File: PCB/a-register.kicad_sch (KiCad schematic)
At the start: 23 parts, among them U48 74LS245, U49 74LS173, U50 74LS173

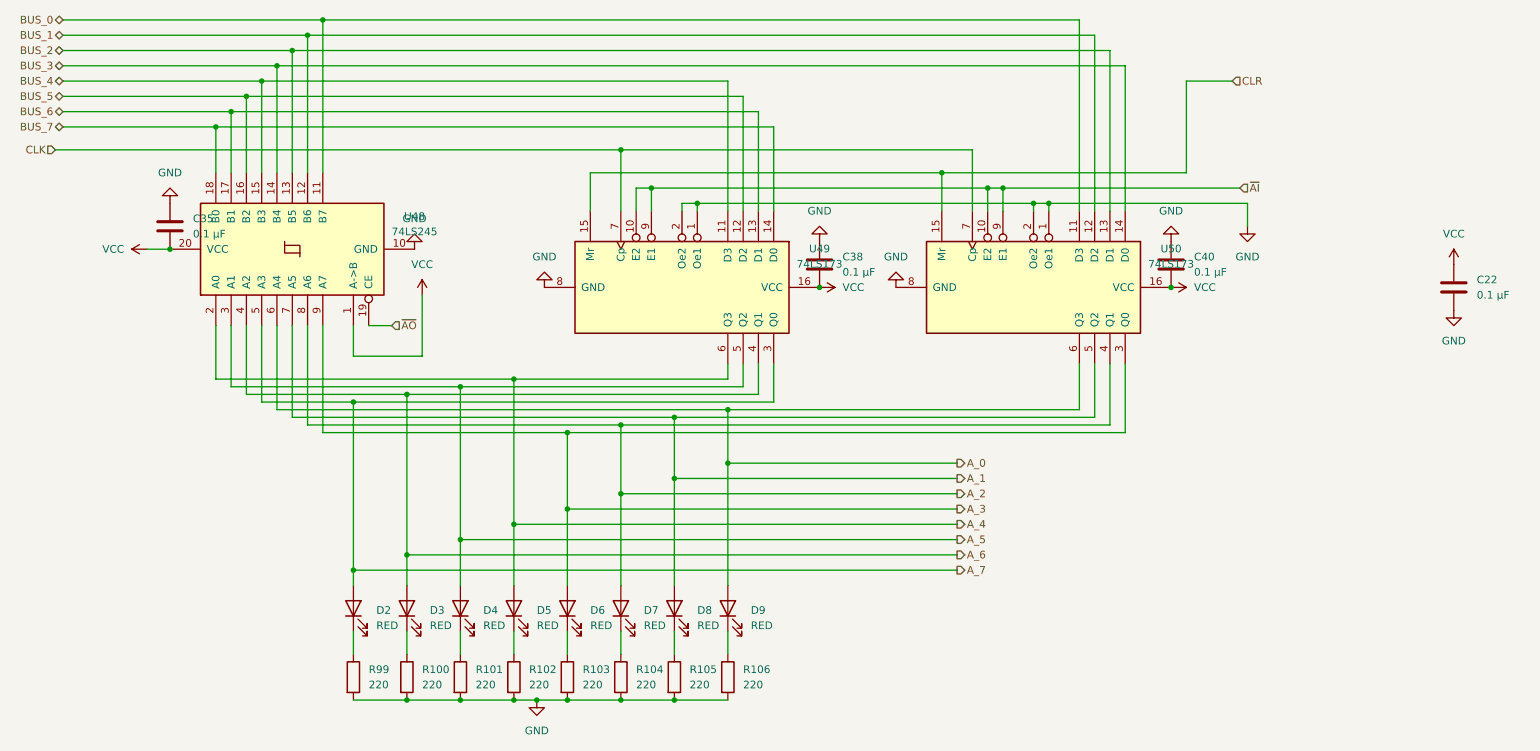
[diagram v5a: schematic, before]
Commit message: Redoing PCB layout and fixed some signal flow convention errors
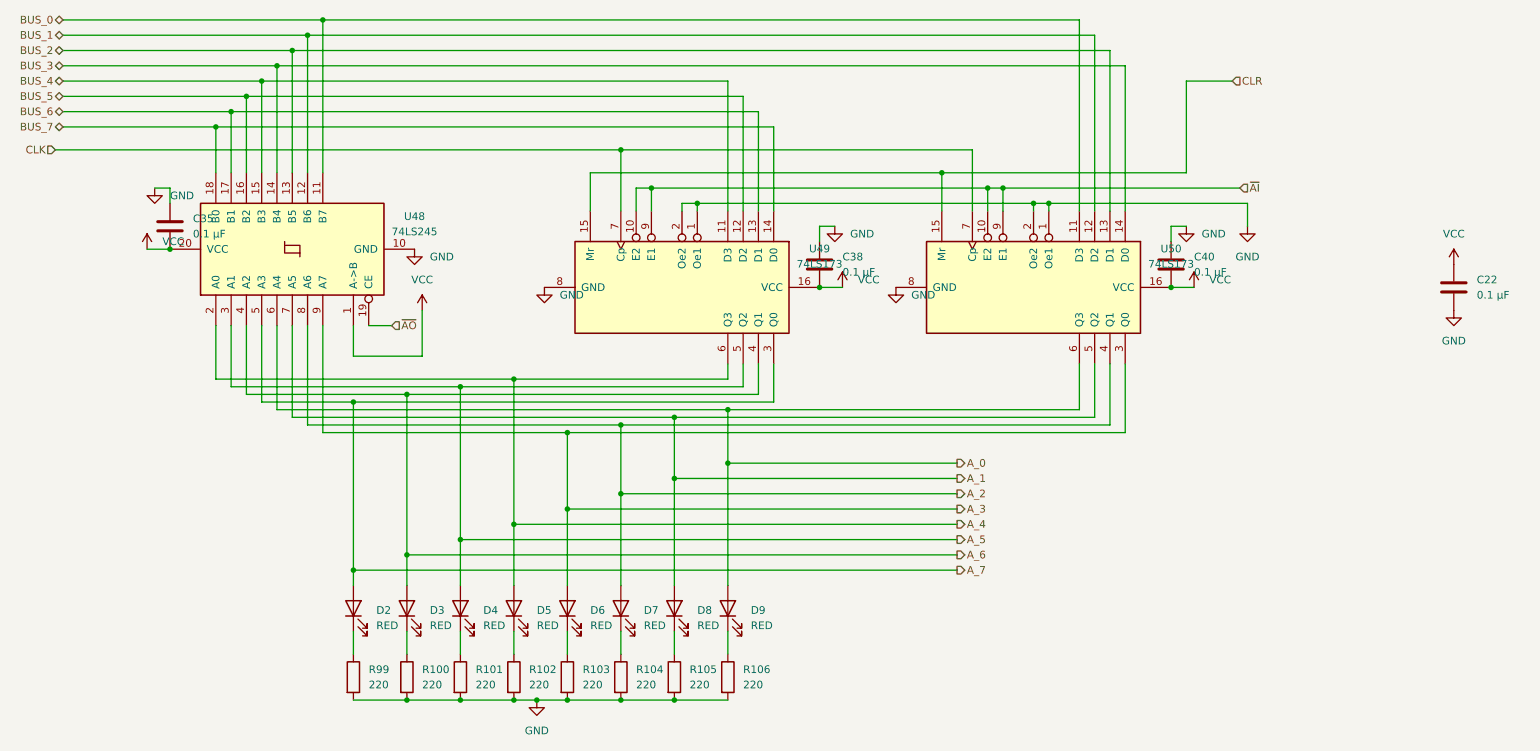
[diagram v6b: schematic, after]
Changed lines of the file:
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@@
 	(wire
 		(pts
+			(xy 217.17 64.77) (xy 213.36 64.77)
+		)
+		(stroke
+			(width 0)
+			(type default)
+		)
+	)
+	(wire
+		(pts
 			(xy 121.92 121.92) (xy 121.92 125.73)
 		)
@@
 	(wire
 		(pts
+			(xy 157.48 54.61) (xy 154.94 54.61)
+		)
+		(stroke
+			(width 0)
+			(type default)
+		)
+	)
+	(wire
+		(pts
 			(xy 104.14 121.92) (xy 104.14 125.73)
 		)
@@
 	(wire
 		(pts
+			(xy 154.94 54.61) (xy 154.94 57.15)
+		)
+		(stroke
+			(width 0)
+			(type default)
+		)
+	)
+	(wire
+		(pts
+			(xy 46.99 48.26) (xy 46.99 50.8)
+		)
+		(stroke
+			(width 0)
+			(type default)
+		)
+	)
+	(wire
+		(pts
 			(xy 203.2 25.4) (xy 203.2 52.07)
 		)
@@
 	(wire
 		(pts
+			(xy 158.75 64.77) (xy 154.94 64.77)
+		)
+		(stroke
+			(width 0)
+			(type default)
+		)
+	)
+	(wire
+		(pts
 			(xy 59.69 33.02) (xy 59.69 45.72)
 		)
@@
 	(wire
 		(pts
+			(xy 44.45 48.26) (xy 46.99 48.26)
+		)
+		(stroke
+			(width 0)
+			(type default)
+		)
+	)
+	(wire
+		(pts
 			(xy 67.31 25.4) (xy 203.2 25.4)
 		)
@@
 	(wire
 		(pts
+			(xy 213.36 54.61) (xy 213.36 57.15)
+		)
+		(stroke
+			(width 0)
+			(type default)
+		)
+	)
+	(wire
+		(pts
 			(xy 69.85 22.86) (xy 69.85 45.72)
 		)
@@
 	(wire
 		(pts
-			(xy 88.9 76.2) (xy 88.9 66.04)
+			(xy 88.9 76.2) (xy 88.9 68.58)
 		)
 		(stroke
@@
 	(wire
 		(pts
+			(xy 215.9 54.61) (xy 213.36 54.61)
+		)
+		(stroke
+			(width 0)
+			(type default)
+		)
+	)
+	(wire
+		(pts
 			(xy 116.84 52.07) (xy 116.84 45.72)
 		)
@@
 	(symbol
 		(lib_id "power:GND")
-		(at 109.22 64.77 180)
+		(at 109.22 64.77 0)
 		(unit 1)
 		(exclude_from_sim no)
@@
 		(fields_autoplaced yes)
 		(property "Reference" "#PWR0146"
-			(at 109.22 58.42 0)
+			(at 109.22 71.12 0)
 			(effects
 				(font
@@
 		)
 		(property "Value" "GND"
-			(at 109.22 59.69 0)
+			(at 111.76 66.0399 0)
 			(effects
 				(font
 					(size 1.27 1.27)
 				)
+				(justify left)
 			)
 		)
@@
 	(symbol
 		(lib_id "power:VCC")
-		(at 213.36 64.77 270)
+		(at 217.17 64.77 0)
 		(unit 1)
 		(exclude_from_sim no)
@@
 		(fields_autoplaced yes)
 		(property "Reference" "#PWR0116"
-			(at 209.55 64.77 0)
+			(at 217.17 68.58 0)
 			(effects
 				(font
@@
 		)
 		(property "Value" "VCC"
-			(at 217.17 64.7699 90)
+			(at 219.71 63.4999 0)
 			(effects
 				(font
@@
 		)
 		(property "Footprint" ""
-			(at 213.36 64.77 0)
+			(at 217.17 64.77 0)
 			(effects
 				(font
@@
 		)
 		(property "Datasheet" ""
-			(at 213.36 64.77 0)
+			(at 217.17 64.77 0)
 			(effects
 				(font
@@
 		)
 		(property "Description" "Power symbol creates a global label with name \"VCC\""
-			(at 213.36 64.77 0)
+			(at 217.17 64.77 0)
 			(effects
 				(font
@@
 	(symbol
 		(lib_id "power:GND")
-		(at 87.63 58.42 180)
+		(at 87.63 58.42 0)
 		(unit 1)
 		(exclude_from_sim no)
@@
 		(fields_autoplaced yes)
 		(property "Reference" "#PWR0174"
-			(at 87.63 52.07 0)
+			(at 87.63 64.77 0)
 			(effects
 				(font
@@
 		)
 		(property "Value" "GND"
-			(at 87.63 53.34 0)
+			(at 90.17 59.6899 0)
 			(effects
 				(font
 					(size 1.27 1.27)
 				)
+				(justify left)
 			)
 		)
@@
 	(symbol
 		(lib_id "power:VCC")
-		(at 154.94 64.77 270)
+		(at 158.75 64.77 0)
 		(unit 1)
 		(exclude_from_sim no)
@@
 		(fields_autoplaced yes)
 		(property "Reference" "#PWR0114"
-			(at 151.13 64.77 0)
+			(at 158.75 68.58 0)
 			(effects
 				(font
@@
 		)
 		(property "Value" "VCC"
-			(at 158.75 64.7699 90)
+			(at 161.29 63.4999 0)
 			(effects
 				(font
@@
 		)
 		(property "Footprint" ""
-			(at 154.94 64.77 0)
+			(at 158.75 64.77 0)
 			(effects
 				(font
@@
 		)
 		(property "Datasheet" ""
-			(at 154.94 64.77 0)
+			(at 158.75 64.77 0)
 			(effects
 				(font
@@
 		)
 		(property "Description" "Power symbol creates a global label with name \"VCC\""
-			(at 154.94 64.77 0)
+			(at 158.75 64.77 0)
 			(effects
 				(font
@@
 	(symbol
 		(lib_id "power:GND")
-		(at 46.99 50.8 180)
+		(at 44.45 48.26 0)
 		(unit 1)
 		(exclude_from_sim no)
@@
 		(fields_autoplaced yes)
 		(property "Reference" "#PWR0147"
-			(at 46.99 44.45 0)
+			(at 44.45 54.61 0)
 			(effects
 				(font
@@
 		)
 		(property "Value" "GND"
-			(at 46.99 45.72 0)
+			(at 46.99 49.5299 0)
 			(effects
 				(font
 					(size 1.27 1.27)
 				)
+				(justify left)
 			)
 		)
 		(property "Footprint" ""
-			(at 46.99 50.8 0)
+			(at 44.45 48.26 0)
 			(effects
 				(font
@@
 		)
 		(property "Datasheet" ""
-			(at 46.99 50.8 0)
+			(at 44.45 48.26 0)
 			(effects
 				(font
@@
 		)
 		(property "Description" "Power symbol creates a global label with name \"GND\" , ground"
-			(at 46.99 50.8 0)
+			(at 44.45 48.26 0)
 			(effects
 				(font
@@
 	(symbol
 		(lib_id "power:VCC")
-		(at 43.18 58.42 90)
+		(at 43.18 58.42 0)
 		(unit 1)
 		(exclude_from_sim no)
@@
 		(fields_autoplaced yes)
 		(property "Reference" "#PWR0117"
-			(at 46.99 58.42 0)
+			(at 43.18 62.23 0)
 			(effects
 				(font
@@
 		)
 		(property "Value" "VCC"
-			(at 39.37 58.4199 90)
+			(at 45.72 57.1499 0)
 			(effects
 				(font
@@
 	(symbol
 		(lib_id "power:GND")
-		(at 167.64 64.77 180)
+		(at 167.64 64.77 0)
 		(unit 1)
 		(exclude_from_sim no)
@@
 		(fields_autoplaced yes)
 		(property "Reference" "#PWR0119"
-			(at 167.64 58.42 0)
+			(at 167.64 71.12 0)
 			(effects
 				(font
@@
 		)
 		(property "Value" "GND"
-			(at 167.64 59.69 0)
+			(at 170.18 66.0399 0)
 			(effects
 				(font
 					(size 1.27 1.27)
 				)
+				(justify left)
 			)
 		)
@@
 	(symbol
 		(lib_id "power:GND")
-		(at 213.36 57.15 180)
+		(at 215.9 54.61 0)
 		(unit 1)
 		(exclude_from_sim no)
@@
 		(fields_autoplaced yes)
 		(property "Reference" "#PWR0176"
-			(at 213.36 50.8 0)
+			(at 215.9 60.96 0)
 			(effects
 				(font
@@
 		)
 		(property "Value" "GND"
-			(at 213.36 52.07 0)
+			(at 218.44 55.8799 0)
 			(effects
 				(font
 					(size 1.27 1.27)
 				)
+				(justify left)
 			)
 		)
 		(property "Footprint" ""
-			(at 213.36 57.15 0)
+			(at 215.9 54.61 0)
 			(effects
 				(font
@@
 		)
 		(property "Datasheet" ""
-			(at 213.36 57.15 0)
+			(at 215.9 54.61 0)
 			(effects
 				(font
@@
 		)
 		(property "Description" "Power symbol creates a global label with name \"GND\" , ground"
-			(at 213.36 57.15 0)
+			(at 215.9 54.61 0)
 			(effects
 				(font
@@
 	(symbol
 		(lib_id "power:GND")
-		(at 154.94 57.15 180)
+		(at 157.48 54.61 0)
 		(unit 1)
 		(exclude_from_sim no)
@@
 		(fields_autoplaced yes)
 		(property "Reference" "#PWR0175"
-			(at 154.94 50.8 0)
+			(at 157.48 60.96 0)
 			(effects
 				(font
@@
 		)
 		(property "Value" "GND"
-			(at 154.94 52.07 0)
+			(at 160.02 55.8799 0)
 			(effects
 				(font
 					(size 1.27 1.27)
 				)
+				(justify left)
 			)
 		)
 		(property "Footprint" ""
-			(at 154.94 57.15 0)
+			(at 157.48 54.61 0)
 			(effects
 				(font
@@
 		)
 		(property "Datasheet" ""
-			(at 154.94 57.15 0)
+			(at 157.48 54.61 0)
 			(effects
 				(font
@@
 		)
 		(property "Description" "Power symbol creates a global label with name \"GND\" , ground"
-			(at 154.94 57.15 0)
+			(at 157.48 54.61 0)
 			(effects
 				(font
@@
 	(symbol
 		(lib_id "power:VCC")
-		(at 88.9 66.04 0)
+		(at 88.9 68.58 0)
 		(unit 1)
 		(exclude_from_sim no)
@@
 		(fields_autoplaced yes)
 		(property "Reference" "#PWR0106"
-			(at 88.9 69.85 0)
+			(at 88.9 72.39 0)
 			(effects
 				(font
@@
 		)
 		(property "Value" "VCC"
-			(at 88.9 60.96 0)
+			(at 88.9 63.5 0)
 			(effects
 				(font
@@
 		)
 		(property "Footprint" ""
-			(at 88.9 66.04 0)
+			(at 88.9 68.58 0)
 			(effects
 				(font
@@
 		)
 		(property "Datasheet" ""
-			(at 88.9 66.04 0)
+			(at 88.9 68.58 0)
 			(effects
 				(font
@@
 		)
 		(property "Description" "Power symbol creates a global label with name \"VCC\""
-			(at 88.9 66.04 0)
+			(at 88.9 68.58 0)
 			(effects
 				(font
